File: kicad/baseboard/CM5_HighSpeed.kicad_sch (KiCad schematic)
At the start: 6 parts, among them J16 Conn_01x22_Female, J5 Conn_01x22_Female

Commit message: Baseboard partial routing
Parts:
- added R14: 2.2K 1%, Resistor_SMD:R_0402_1005Metric, symbol Device:R
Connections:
- net +3.3v: now also R14.1
- net CAM_GPIO0: no longer names the net of J5.17 (Pin_17)
- net CAM_GPIO0: now also R14.2
- net CAM_GPIO1: no longer names the net of J5.18 (Pin_18)
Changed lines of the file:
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@@
 	(wire
 		(pts
+			(xy 135.89 66.04) (xy 128.27 66.04)
+		)
+		(stroke
+			(width 0)
+			(type default)
+		)
+	)
+	(wire
+		(pts
 			(xy 38.1 147.32) (xy 35.56 147.32)
 		)
@@
 	(wire
 		(pts
+			(xy 128.27 66.04) (xy 128.27 64.77)
+		)
+		(stroke
+			(width 0)
+			(type default)
+		)
+	)
+	(wire
+		(pts
 			(xy 134.62 99.06) (xy 151.13 99.06)
 		)
@@
 		)
 	)
+	(label "+3.3v"
+		(at 128.27 64.77 0)
+		(effects
+			(font
+				(size 1.27 1.27)
+			)
+			(justify left bottom)
+		)
+	)
 	(label "DPHY0_D0_P"
 		(at 134.62 30.48 0)
@@
 		)
 	)
-	(hierarchical_label "CAM_GPIO0"
-		(shape input)
-		(at 143.51 66.04 180)
-		(effects
-			(font
-				(size 1.27 1.27)
-			)
-			(justify right)
-		)
-	)
 	(hierarchical_label "PCIE_RX_N"
 		(shape input)
@@
 		)
 	)
-	(hierarchical_label "CAM_GPIO1"
-		(shape input)
-		(at 143.51 68.58 180)
-		(effects
-			(font
-				(size 1.27 1.27)
-			)
-			(justify right)
-		)
-	)
 	(hierarchical_label "PCIE_TX_N"
 		(shape output)
@@
 					(unit 1)
 				)
+			)
+		)
+	)
+	(symbol
+		(lib_id "Device:R")
+		(at 139.7 66.04 90)
+		(unit 1)
+		(exclude_from_sim no)
+		(in_bom yes)
+		(on_board yes)
+		(dnp no)
+		(property "Reference" "R14"
+			(at 137.795 63.5 90)
+			(effects
+				(font
+					(size 1.27 1.27)
+				)
+				(justify left)
+			)
+		)
+		(property "Value" "2.2K 1%"
+			(at 146.05 63.5 90)
+			(effects
+				(font
+					(size 1.27 1.27)
+				)
+				(justify left)
+			)
+		)
+		(property "Footprint" "Resistor_SMD:R_0402_1005Metric"
+			(at 139.7 67.818 90)
+			(effects
+				(font
+					(size 1.27 1.27)
+				)
+				(hide yes)
+			)
+		)
+		(property "Datasheet" "https://fscdn.rohm.com/en/products/databook/datasheet/passive/resistor/chip_resistor/mcr-e.pdf"
+			(at 139.7 66.04 0)
+			(effects
+				(font
+					(size 1.27 1.27)
+				)
+				(hide yes)
+			)
+		)
+		(property "Description" ""
+			(at 139.7 66.04 0)
+			(effects
+				(font
+					(size 1.27 1.27)
+				)
+				(hide yes)
+			)
+		)
+		(property "Field4" "Farnell"
+			(at 139.7 66.04 0)
+			(effects
+				(font
+					(size 1.27 1.27)
+				)
+				(hide yes)
+			)
+		)
+		(property "Field5" ""
+			(at 139.7 66.04 0)
+			(effects
+				(font
+					(size 1.27 1.27)
+				)
+				(hide yes)
+			)
+		)
+		(property "Field7" ""
+			(at 139.7 66.04 0)
+			(effects
+				(font
+					(size 1.27 1.27)
+				)
+				(hide yes)
+			)
+		)
+		(property "Field6" ""
+			(at 139.7 66.04 0)
+			(effects
+				(font
+					(size 1.27 1.27)
+				)
+				(hide yes)
+			)
+		)
+		(property "Part Description" "Resistor 2.2K M1005 1% 63mW"
+			(at 139.7 66.04 0)
+			(effects
+				(font
+					(size 1.27 1.27)
+				)
+				(hide yes)
+			)
+		)
+		(property "Field8" ""
+			(at 139.7 66.04 0)
+			(effects
+				(font
+					(size 1.27 1.27)
+				)
+				(hide yes)
+			)
+		)
+		(pin "1"
+		)
+		(pin "2"
+		)
+		(instances
+			(project "baseboard"
+				(path "/e63e39d7-6ac0-4ffd-8aa3-1841a4541b55/00000000-0000-0000-0000-00005cff70b1"
+					(reference "R14")
+					(unit 1)
+				)

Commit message: Finish PCB routing
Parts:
- R14: footprint Resistor_SMD:R_0402_1005Metric -> Resistor_SMD:R_0603_1608Metric; Field4 Farnell -> (none); LCSC Part # (none) -> LCSC Part #
- R6, R7: footprint Resistor_SMD:R_0402_1005Metric -> Resistor_SMD:R_0603_1608Metric
- R8: footprint Resistor_SMD:R_0402_1005Metric -> Resistor_SMD:R_0603_1608Metric; Field4 Farnell -> (none); LCSC Part # (none) -> C4190
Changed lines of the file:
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@@
 			)
 		)
-		(property "Footprint" "Resistor_SMD:R_0402_1005Metric"
+		(property "Footprint" "Resistor_SMD:R_0603_1608Metric"
 			(at 200.152 64.77 90)
 			(effects
@@
 			)
 		)
-		(property "Footprint" "Resistor_SMD:R_0402_1005Metric"
+		(property "Footprint" "Resistor_SMD:R_0603_1608Metric"
 			(at 207.772 64.77 90)
 			(effects
@@
 			)
 		)
-		(property "Footprint" "Resistor_SMD:R_0402_1005Metric"
+		(property "Footprint" "Resistor_SMD:R_0603_1608Metric"
 			(at 138.43 138.938 90)
 			(effects
@@
 			)
 		)
-		(property "Field4" "Farnell"
-			(at 138.43 137.16 0)
-			(effects
-				(font
-					(size 1.27 1.27)
-				)
-				(hide yes)
-			)
-		)
-		(property "Field5" ""
-			(at 138.43 137.16 0)
-			(effects
-				(font
-					(size 1.27 1.27)
-				)
-				(hide yes)
-			)
-		)
-		(property "Field7" ""
-			(at 138.43 137.16 0)
-			(effects
-				(font
-					(size 1.27 1.27)
-				)
-				(hide yes)
-			)
-		)
-		(property "Field6" ""
-			(at 138.43 137.16 0)
-			(effects
-				(font
-					(size 1.27 1.27)
-				)
-				(hide yes)
-			)
-		)
 		(property "Part Description" "Resistor 2.2K M1005 1% 63mW"
 			(at 138.43 137.16 0)
@@
 			)
 		)
-		(property "Field8" ""
-			(at 138.43 137.16 0)
+		(property "LCSC Part #" "C4190"
+			(at 138.43 137.16 90)
 			(effects
 				(font
@@
 			)
 		)
-		(property "Footprint" "Resistor_SMD:R_0402_1005Metric"
+		(property "Footprint" "Resistor_SMD:R_0603_1608Metric"
 			(at 139.7 67.818 90)
 			(effects
@@
 			)
 		)
-		(property "Field4" "Farnell"
-			(at 139.7 66.04 0)
-			(effects
-				(font
-					(size 1.27 1.27)
-				)
-				(hide yes)
-			)
-		)
-		(property "Field5" ""
-			(at 139.7 66.04 0)
-			(effects
-				(font
-					(size 1.27 1.27)
-				)
-				(hide yes)
-			)
-		)
-		(property "Field7" ""
-			(at 139.7 66.04 0)
-			(effects
-				(font
-					(size 1.27 1.27)
-				)
-				(hide yes)
-			)
-		)
-		(property "Field6" ""
-			(at 139.7 66.04 0)
-			(effects
-				(font
-					(size 1.27 1.27)
-				)
-				(hide yes)
-			)
-		)
 		(property "Part Description" "Resistor 2.2K M1005 1% 63mW"
 			(at 139.7 66.04 0)
@@
 			)
 		)
-		(property "Field8" ""
-			(at 139.7 66.04 0)
-			(effects
-				(font
+		(property "LCSC Part #" "LCSC Part #"
+			(at 139.7 66.04 90)
+			(effects
+				(font

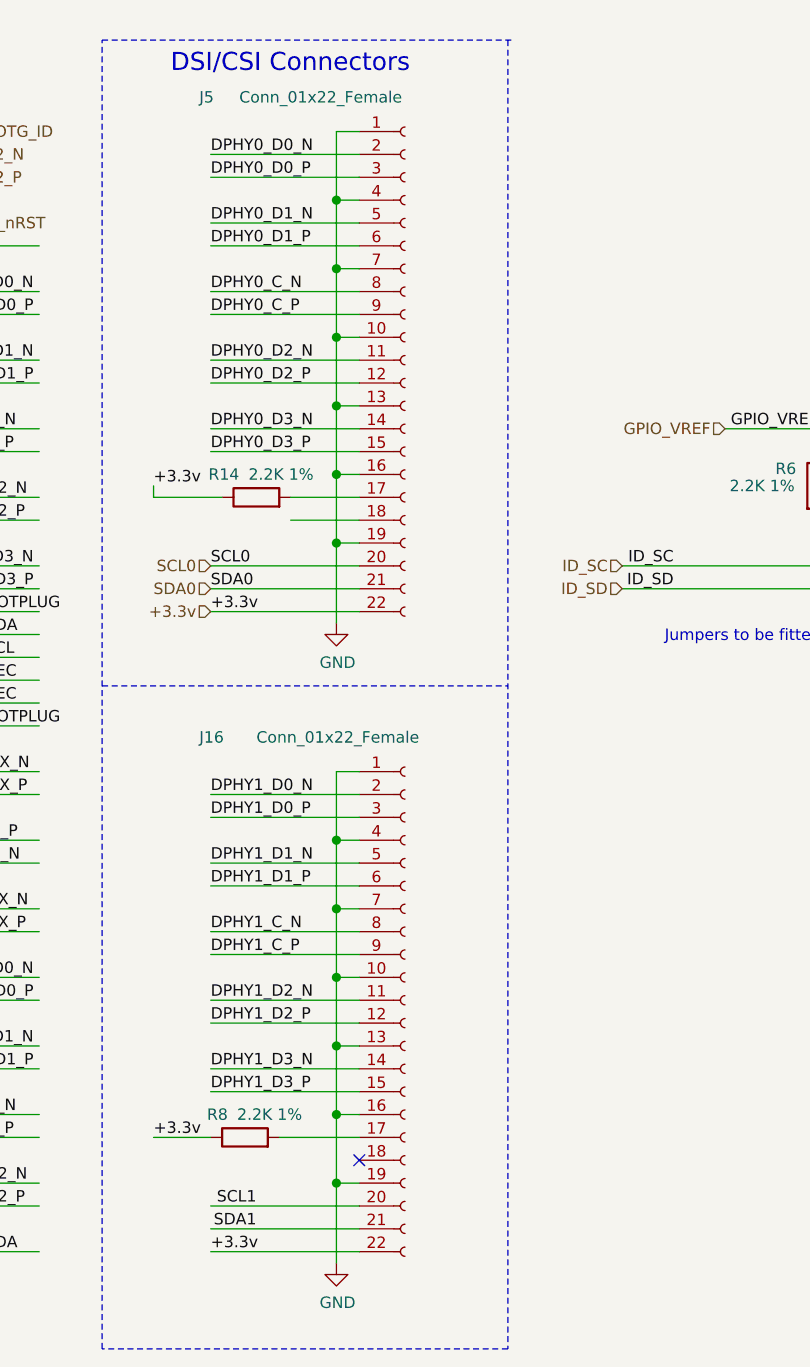
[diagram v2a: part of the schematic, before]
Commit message: Correct V1 mistakes : Turned MISO, Correct STM32 template.   Add BMO055 Gyroskope . Add servo connector. Add serial port connector. Add Pi - Stm32 serial connection. Add Silkscreen texts.
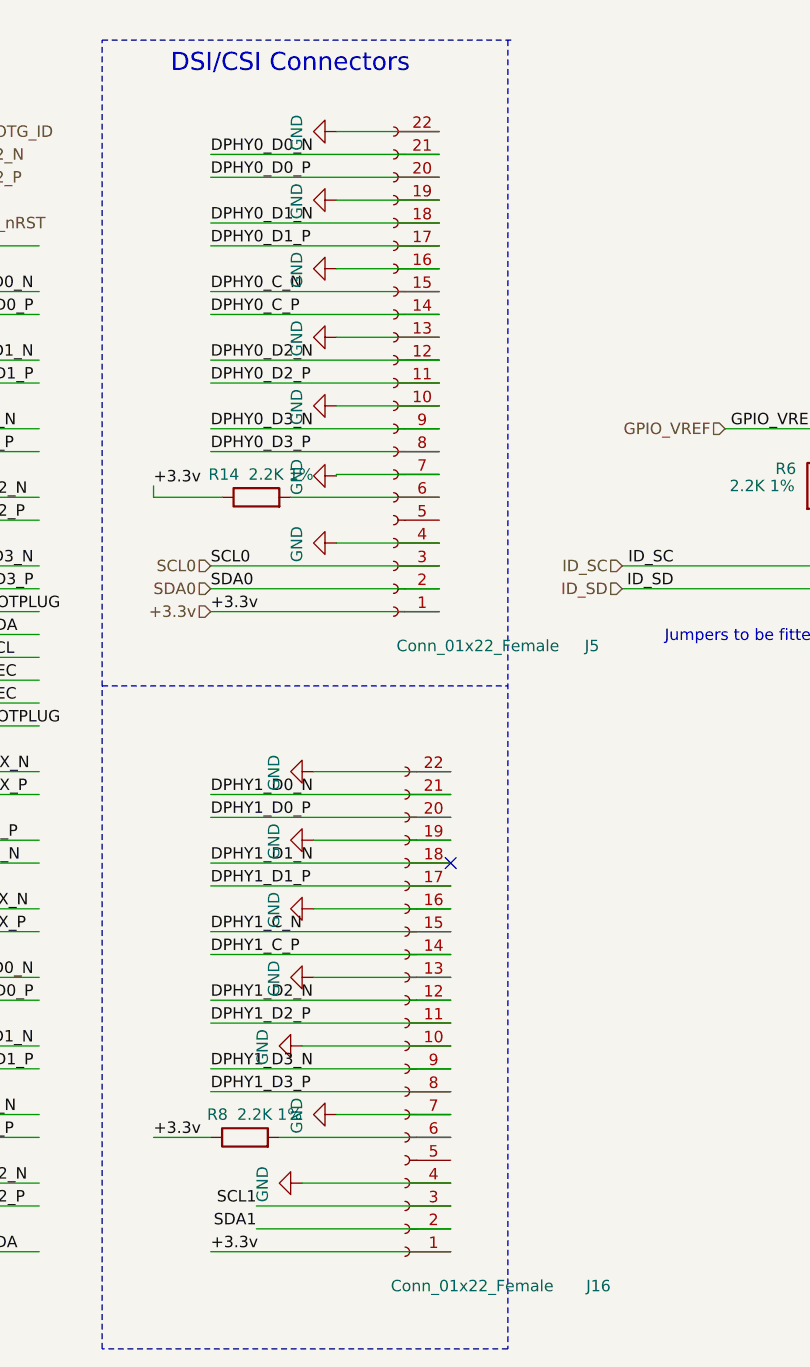
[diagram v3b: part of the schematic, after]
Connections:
- net +3.3v: now also J16.1 (Pin_1), J5.1 (Pin_1); no longer J16.22 (Pin_22), J5.22 (Pin_22)
- net DPHY0_C_N: now also J5.15 (Pin_15); no longer J5.8 (Pin_8)
- net DPHY0_C_P: now also J5.14 (Pin_14); no longer J5.9 (Pin_9)
- net DPHY0_D0_N: now also J5.21 (Pin_21); no longer J5.2 (Pin_2)
- net DPHY0_D0_P: now also J5.20 (Pin_20); no longer J5.3 (Pin_3)
- net DPHY0_D1_N: now also J5.18 (Pin_18); no longer J5.5 (Pin_5)
- net DPHY0_D1_P: now also J5.17 (Pin_17); no longer J5.6 (Pin_6)
- net DPHY0_D2_N: now also J5.12 (Pin_12); no longer J5.11 (Pin_11)
- net DPHY0_D2_P: now also J5.11 (Pin_11); no longer J5.12 (Pin_12)
- net DPHY0_D3_N: now also J5.9 (Pin_9); no longer J5.14 (Pin_14)
- net DPHY0_D3_P: now also J5.8 (Pin_8); no longer J5.15 (Pin_15)
- net DPHY1_C_N: now also J16.15 (Pin_15); no longer J16.8 (Pin_8)
- net DPHY1_C_P: now also J16.14 (Pin_14); no longer J16.9 (Pin_9)
- net DPHY1_D0_N: now also J16.21 (Pin_21); no longer J16.2 (Pin_2)
- net DPHY1_D0_P: now also J16.20 (Pin_20); no longer J16.3 (Pin_3)
- net DPHY1_D1_N: now also J16.18 (Pin_18); no longer J16.5 (Pin_5)
- net DPHY1_D1_P: now also J16.17 (Pin_17); no longer J16.6 (Pin_6)
- net DPHY1_D2_N: now also J16.12 (Pin_12); no longer J16.11 (Pin_11)
- net DPHY1_D2_P: now also J16.11 (Pin_11); no longer J16.12 (Pin_12)
- net DPHY1_D3_N: now also J16.9 (Pin_9); no longer J16.14 (Pin_14)
- net DPHY1_D3_P: now also J16.8 (Pin_8); no longer J16.15 (Pin_15)
- net GND: now also J16.22 (Pin_22), J5.22 (Pin_22); no longer J16.1 (Pin_1), J5.1 (Pin_1)
- net ID_SC: now also J16.3 (Pin_3); no longer J16.20 (Pin_20)
- net ID_SD: now also J16.2 (Pin_2); no longer J16.21 (Pin_21)
- net SCL0: now also J5.3 (Pin_3); no longer J5.20 (Pin_20)
- net SDA0: now also J5.2 (Pin_2); no longer J5.21 (Pin_21)
- net at R14.2: now also J5.6 (Pin_6); no longer J5.17 (Pin_17)
- net at R8.2: now also J16.6 (Pin_6); no longer J16.17 (Pin_17)
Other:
- moved on the sheet: J16, J5
